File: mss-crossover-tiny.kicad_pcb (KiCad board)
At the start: 2 copper layers, 50.8 x 71.6 mm, 35 parts, among them J1 2x-screw, J2 RJ45, J3 2x-screw, J4 2x-screw, J5 ISP--5V, J6 TagConnect, J7 RJ45, SW1 Set, U1 L78M05CDT, U2 ACS724xLCTR-05AB, U3 ATtiny25-20SS, U4 AD8603, U5 LTV-355T

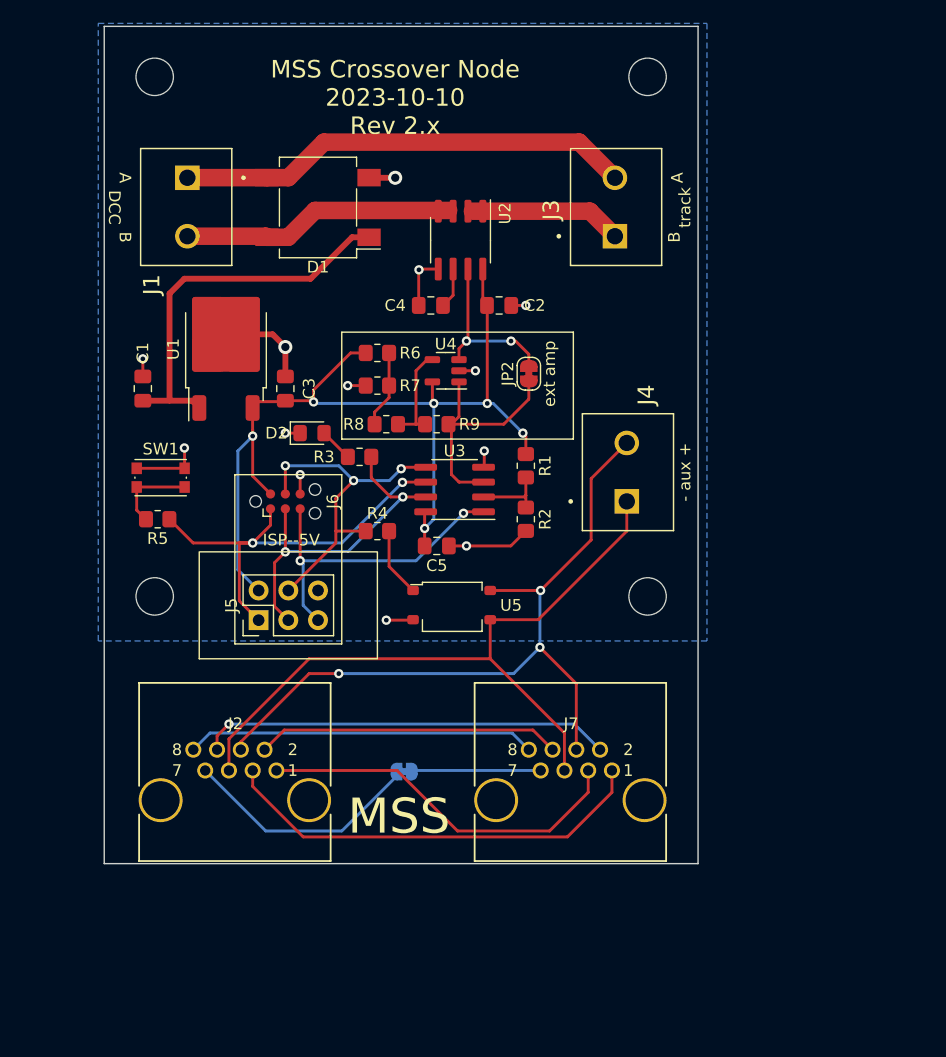
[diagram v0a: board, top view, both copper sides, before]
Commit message: Added test points to board.  In src, added code to control the opto-isolator as well as the LED.
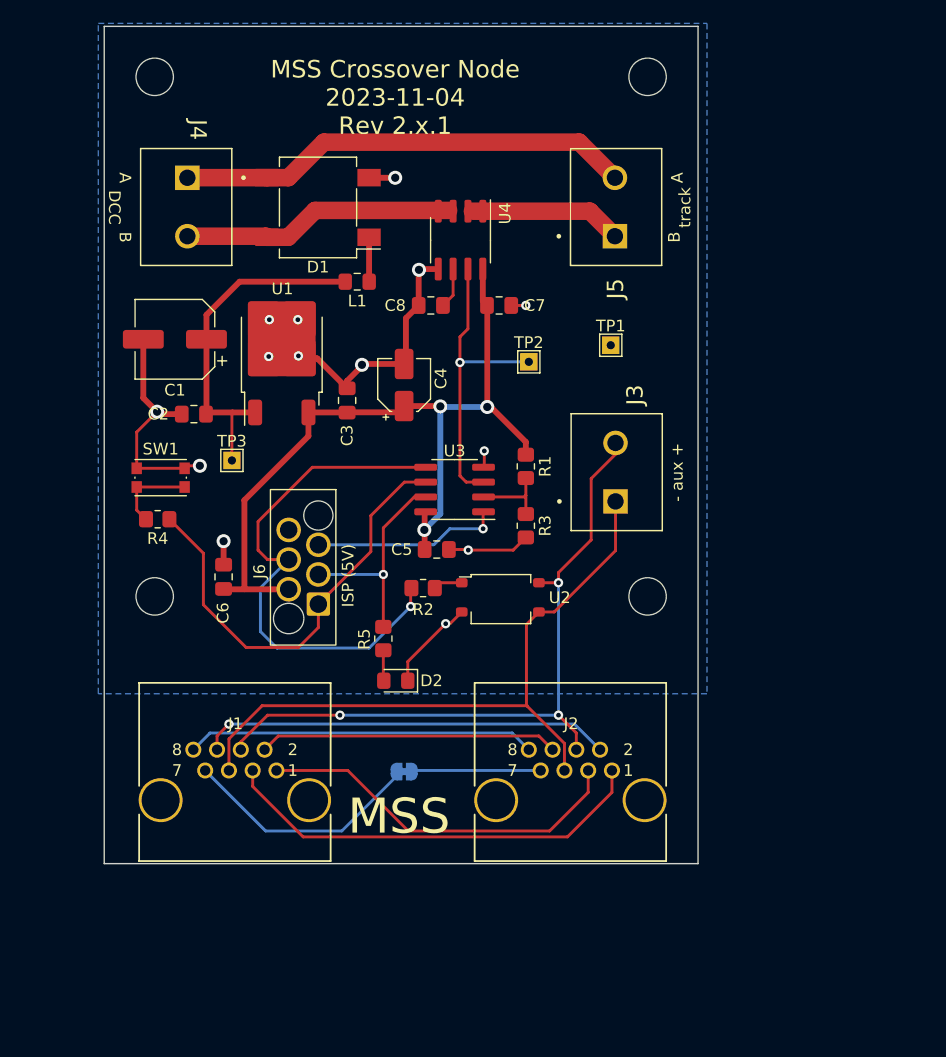
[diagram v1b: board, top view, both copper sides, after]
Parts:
- removed the J6 at (121.4, 96.3)
- removed JP2: ext amp, Jumper:SolderJumper-2_P1.3mm_Bridged_RoundedPad1.0x1.5mm
- removed R6, R7, R8, R9: 39k, Resistor_SMD:R_0805_2012Metric_Pad1.20x1.40mm_HandSolder
- removed the U4 at (135.1, 85.1)
- added C1: 47µF, Capacitor_SMD:CP_Elec_6.3x5.7, F.Cu at (112.0, 82.4)
- added C4: 10µF, Capacitor_SMD:CP_Elec_4x5.7, F.Cu at (131.6, 86.3)
- added C6: 100nF, Capacitor_SMD:C_0805_2012Metric_Pad1.18x1.45mm_HandSolder, F.Cu at (116.1, 102.7)
- added L1: L, Inductor_SMD:L_0805_2012Metric_Pad1.15x1.40mm_HandSolder, F.Cu at (127.6, 77.5)
- added TP1: TestPoint, TestPoint:TestPoint_THTPad_1.5x1.5mm_Drill0.7mm, F.Cu at (149.3, 82.9)
- added TP2: TestPoint, TestPoint:TestPoint_THTPad_1.5x1.5mm_Drill0.7mm, F.Cu at (142.2, 84.3)
- added TP3: TestPoint, TestPoint:TestPoint_THTPad_1.5x1.5mm_Drill0.7mm, F.Cu at (116.8, 92.8)
- C8: renamed from C4; value 1nF -> 3.3nF
- J6: renamed from J5; value ISP--5V -> ISP (5V); footprint myMods:PinHeader_2x03_P2.54mm_Vertical_Shrouded -> myMods:skedd-6-debugging
- R4: renamed from R5; value 2.2k -> 4.7k
- R5: renamed from R3; value 2.2k -> 4.7k
- moved D2 22.4 mm to (130.9, 111.6), turned to 180 degrees
- moved R5 15.7 mm to (129.8, 108.0), turned to -90 degrees
- moved R2 6.25 mm to (133.2, 103.7)
- moved C3 5.38 mm to (126.7, 87.6)
- moved J6 5.29 mm to (124.2, 105.1), turned to -90 degrees
- moved C2 4.88 mm to (113.6, 88.8), turned to 180 degrees
- moved U1 4.79 mm to (121.1, 83.6)
- moved U2 4.22 mm to (143.1, 103.2)
- moved J3 0.97 mm to (149.7, 96.3)
- moved R3 0.56 mm to (142.0, 98.3)
- moved C5 0.30 mm to (134.4, 100.4)
- moved R1 0.05 mm to (142.0, 93.3)
- renumbered C1 to C2, C2 to C7, J2 to J1, J7 to J2, J4 to J3, J1 to J4, J3 to J5, R4 to R2, R2 to R3, U5 to U2, U2 to U4
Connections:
- C2 pad 1: Net-(D1-+) -> Net-(U1-Input)
- U1 pad 1: Net-(D1-+) -> Net-(U1-Input)
- U3 pad 3: Net-(JP2-A) -> Net-(U3-XTAL2/PB4)
- U4 pad 7: Net-(JP2-B) -> Net-(U3-XTAL2/PB4)
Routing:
- net Net-(U1-Input): track 0.00 -> 29.9 mm
- net Net-(D1-+): track 33.3 -> 3.80 mm
- net Net-(U3-XTAL2/PB4): track 0.00 -> 26.1 mm, vias 0 -> 1
- net GND: track 40.2 -> 63.4 mm, vias 13 -> 14
- net Net-(JP2-A): track 20.2 -> 0.00 mm
- net /MOSI: track 29.7 -> 45.3 mm, vias 3 -> 1
- net Net-(JP2-B): track 14.9 -> 0.00 mm, vias 2 -> 0
- net +5V: track 82.4 -> 69.9 mm, vias 6 -> 3
- net /RST: track 27.6 -> 16.1 mm, vias 2 -> 1
- net /SCK: track 29.5 -> 18.7 mm, vias 2 -> 1
- net Net-(U4--): track 8.30 -> 0.00 mm
- net Net-(R6-Pad2): track 6.61 -> 0.00 mm
- net /Local A: track 64.6 -> 59.4 mm
- net Net-(R2-Pad1): track 5.93 -> 2.50 mm
- net /MSS GND: track 60.8 -> 57.7 mm
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
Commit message: Changed to be able to plug the crossover board into a cascade board.
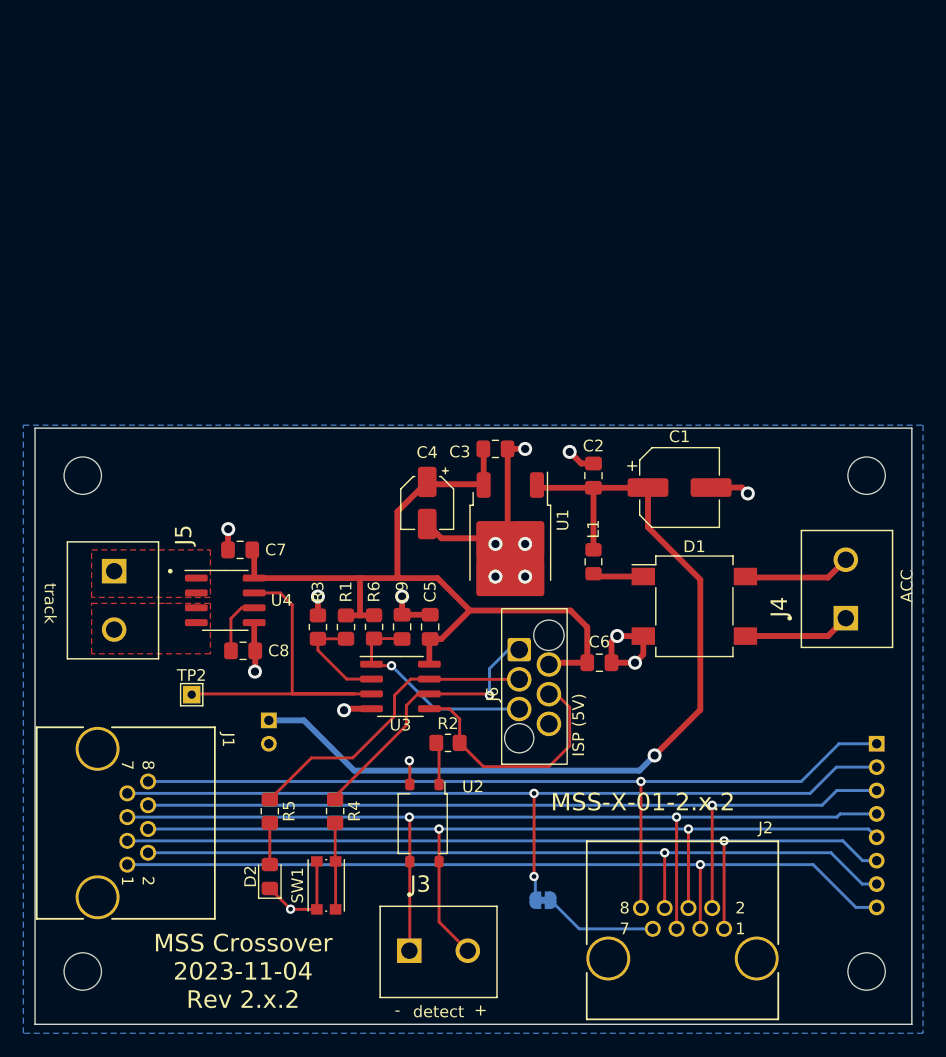
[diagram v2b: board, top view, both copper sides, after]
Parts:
- removed TP1, TP3: TestPoint, TestPoint:TestPoint_THTPad_1.5x1.5mm_Drill0.7mm
- added C9: 1uF, Capacitor_SMD:C_0805_2012Metric_Pad1.18x1.45mm_HandSolder, F.Cu at (131.4, 107.0)
- added J7: Conn_01x10_Pin, Connector_PinHeader_2.00mm:PinHeader_1x08_P2.00mm_Vertical, B.Cu at (172.0, 117.0)
- added J8: Conn_01x02_Pin, Connector_PinHeader_2.00mm:PinHeader_1x02_P2.00mm_Vertical, B.Cu at (120.0, 115.0)
- added R6: 10k, Resistor_SMD:R_0805_2012Metric_Pad1.20x1.40mm_HandSolder, F.Cu at (129.0, 107.0)
- moved J4 67.8 mm to (169.4, 106.3), turned to 90 degrees
- moved J5 51.5 mm to (106.8, 102.2), turned to -90 degrees
- moved D1 46.9 mm to (156.4, 105.2), turned to 0 degrees
- moved C1 45.0 mm to (155.1, 95.1), turned to 0 degrees
- moved J3 42.3 mm to (132.0, 134.7), turned to 0 degrees
- moved TP2 40.5 mm to (113.4, 112.8)
- moved REF** 38.9 mm to (171.1, 94.1)
- moved SW1 37.6 mm to (124.9, 129.1), turned to 90 degrees
- moved REF** 37.2 mm to (171.1, 136.5)
- moved U4 36.8 mm to (116.3, 104.7), turned to 0 degrees
- moved REF** 34.7 mm to (104.1, 94.1)
- moved C2 34.6 mm to (147.8, 94.1), turned to 90 degrees
- moved C8 33.6 mm to (117.8, 109.0), turned to 0 degrees
- moved C6 33.0 mm to (148.3, 110.1), turned to 180 degrees
- moved REF** 32.7 mm to (104.1, 136.5)
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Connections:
- net Net-(J5-Pin_1) renamed /t1
- net Net-(U1-Input) renamed +12V
- J5 pad 2: Net-(J4-Pin_1) -> /t2
- U4 pad 3: Net-(J4-Pin_2) -> /t2
- U4 pad 4: Net-(J4-Pin_2) -> /t2
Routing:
- net /7 A: track 20.8 -> 74.2 mm, vias 0 -> 2
- net +12V: track 29.9 -> 76.6 mm, vias 0 -> 1
- net /AD A: track 29.9 -> 74.5 mm, vias 0 -> 1
- net /Ain A: track 25.6 -> 68.2 mm, vias 0 -> 1
- net /AAin A: track 32.1 -> 71.1 mm, vias 0 -> 1
- net /Ain B: track 35.3 -> 71.6 mm
- net /AAin B: track 37.3 -> 72.3 mm, vias 0 -> 1
- net Net-(J4-Pin_1): track 39.1 -> 9.22 mm
- net /MSS GND: track 57.7 -> 85.2 mm, vias 0 -> 2
- net /MOSI: track 45.3 -> 21.5 mm, vias 1 -> 0
- net /Local A: track 59.4 -> 80.8 mm, vias 3 -> 2
- net /MISO: track 37.9 -> 23.6 mm, vias 0 -> 1
- net Net-(J4-Pin_2): track 23.3 -> 9.25 mm
- net /t1: track 13.1 -> 0.00 mm
- net /SCK: track 18.7 -> 26.7 mm, vias 1 -> 0
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- added copper zone on F.Cu, net /t1
- added copper zone on F.Cu, net /t2
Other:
- board size 50.8 x 71.6 mm -> 75 x 51 mm
- board text added: "MSS Crossover ${ISSUE_DATE} Rev ${REVISION}"
- board text added: "MSS-X-01-${REVISION}"
- board text removed: "MSS"
- board text removed: "MSS Crossover Node ${ISSUE_DATE} Rev ${REVISION}"

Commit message: Little updates.  Moved power from 12V to ACC back to 12V.
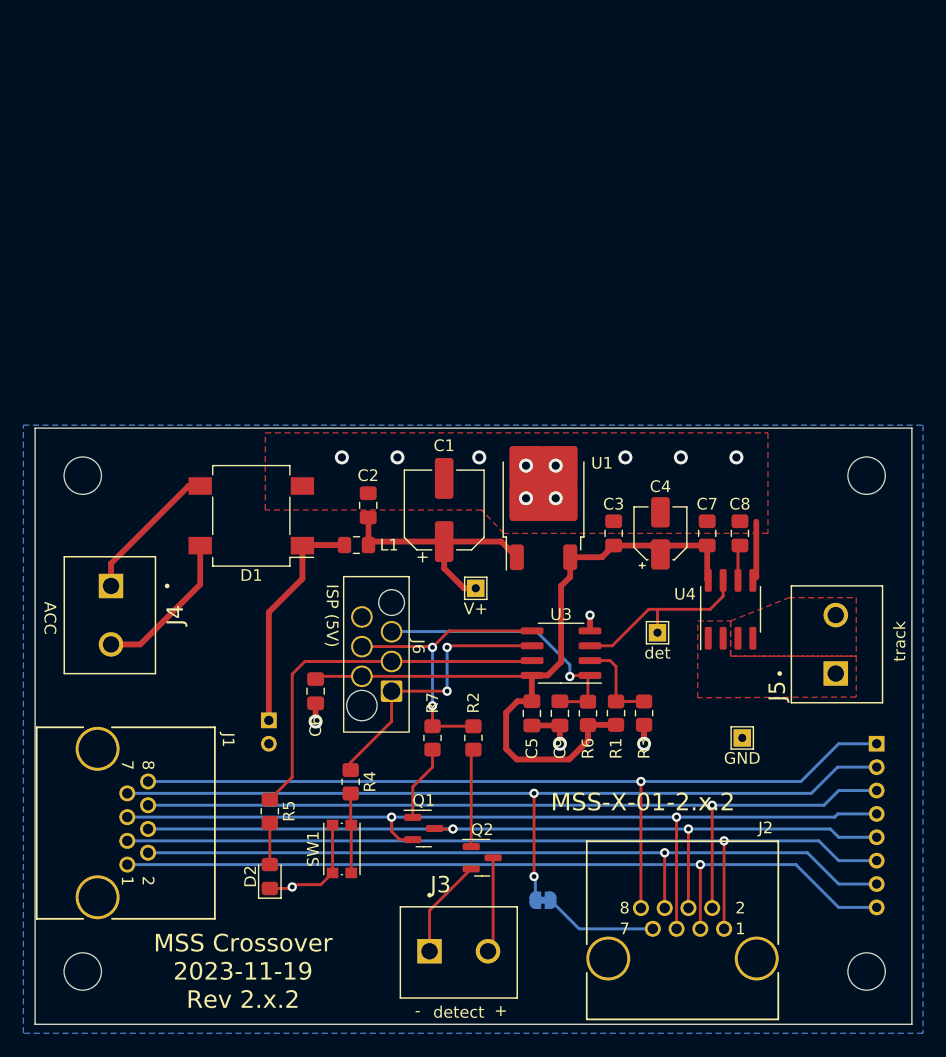
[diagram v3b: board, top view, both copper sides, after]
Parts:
- removed U2: LTV-355T, myMods:LTV-355T
- added Q1: 2N3904, Package_TO_SOT_SMD:SOT-23, F.Cu at (133.2, 124.2)
- added Q2: 2N3904, Package_TO_SOT_SMD:SOT-23, F.Cu at (138.2, 126.8)
- added R7: 2.2k, Resistor_SMD:R_0805_2012Metric_Pad1.20x1.40mm_HandSolder, F.Cu at (134.0, 116.5)
- added TP1: GND, TestPoint:TestPoint_THTPad_1.5x1.5mm_Drill0.7mm, F.Cu at (160.5, 116.5)
- added TP3: V+, TestPoint:TestPoint_THTPad_1.5x1.5mm_Drill0.7mm, F.Cu at (137.7, 103.7)
- R2: value 1k -> 2.2k
- TP2: value TestPoint -> det
- moved J4 62.9 mm to (106.5, 103.5), turned to -90 degrees
- moved J5 62.4 mm to (168.5, 111.0), turned to 90 degrees
- moved C8 43.7 mm to (160.3, 99.0), turned to 90 degrees
- moved U4 43.2 mm to (159.5, 105.5), turned to 90 degrees
- moved TP2 40.2 mm to (153.2, 107.5)
- moved C7 40.0 mm to (157.5, 99.0), turned to -90 degrees
- moved D1 38.7 mm to (118.5, 97.5), turned to 180 degrees
- moved R3 28.9 mm to (152.1, 114.4), turned to -90 degrees
- moved C6 24.4 mm to (124.0, 112.5), turned to 90 degrees
- moved R1 24.2 mm to (149.7, 114.4), turned to 90 degrees
- moved L1 20.3 mm to (127.5, 100.0), turned to 0 degrees
- moved C1 20.2 mm to (135.0, 97.0), turned to 90 degrees
- moved C4 20.1 mm to (153.5, 99.0), turned to 90 degrees
- moved R6 19.7 mm to (147.3, 114.4), turned to 90 degrees
- moved C2 19.4 mm to (128.5, 96.6)
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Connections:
- C1 pad 1: +12V -> Net-(U1-Input)
- C2 pad 1: +12V -> Net-(U1-Input)
- J1 pad 5: /MSS GND -> GND
- J2 pad 5: /MSS GND -> GND
- J3 pad 1: /MSS GND -> GND
- J3 pad 2: /Local A -> Net-(J3-Pin_2)
- J7 pad 4: /MSS GND -> GND
- J8 pad 1: +12V -> Net-(D1-+)
- L1 pad 2: +12V -> Net-(U1-Input)
- R2 pad 1: Net-(R2-Pad1) -> /MOSI
- R2 pad 2: /MOSI -> Net-(Q2-B)
- U1 pad 1: +12V -> Net-(U1-Input)
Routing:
- net /MSS GND: track 85.2 -> 0.00 mm, vias 2 -> 0
- net +12V: track 76.6 -> 0.00 mm, vias 1 -> 0
- net GND: track 56.9 -> 109.3 mm, vias 16 -> 17
- net Net-(U1-Input): track 0.00 -> 21.5 mm
- net Net-(U3-XTAL2/PB4): track 32.0 -> 16.5 mm
- net Net-(D1-+): track 4.36 -> 19.8 mm
- net /Local A: track 80.8 -> 71.0 mm
- net Net-(Q2-B): track 0.00 -> 8.38 mm
- net Net-(J3-Pin_2): track 0.00 -> 8.18 mm
- net Net-(Q1-B): track 0.00 -> 6.50 mm
- net /SCK: track 26.7 -> 32.5 mm
- net /RST: track 18.9 -> 23.5 mm
- net /MOSI: track 21.5 -> 25.4 mm, vias 0 -> 2
- net Net-(J4-Pin_2): track 9.25 -> 13.1 mm
- net Net-(R2-Pad1): track 3.66 -> 0.00 mm
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- added copper zone on F.Cu, net GND

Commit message: Reworked design to use a current shunt instead.
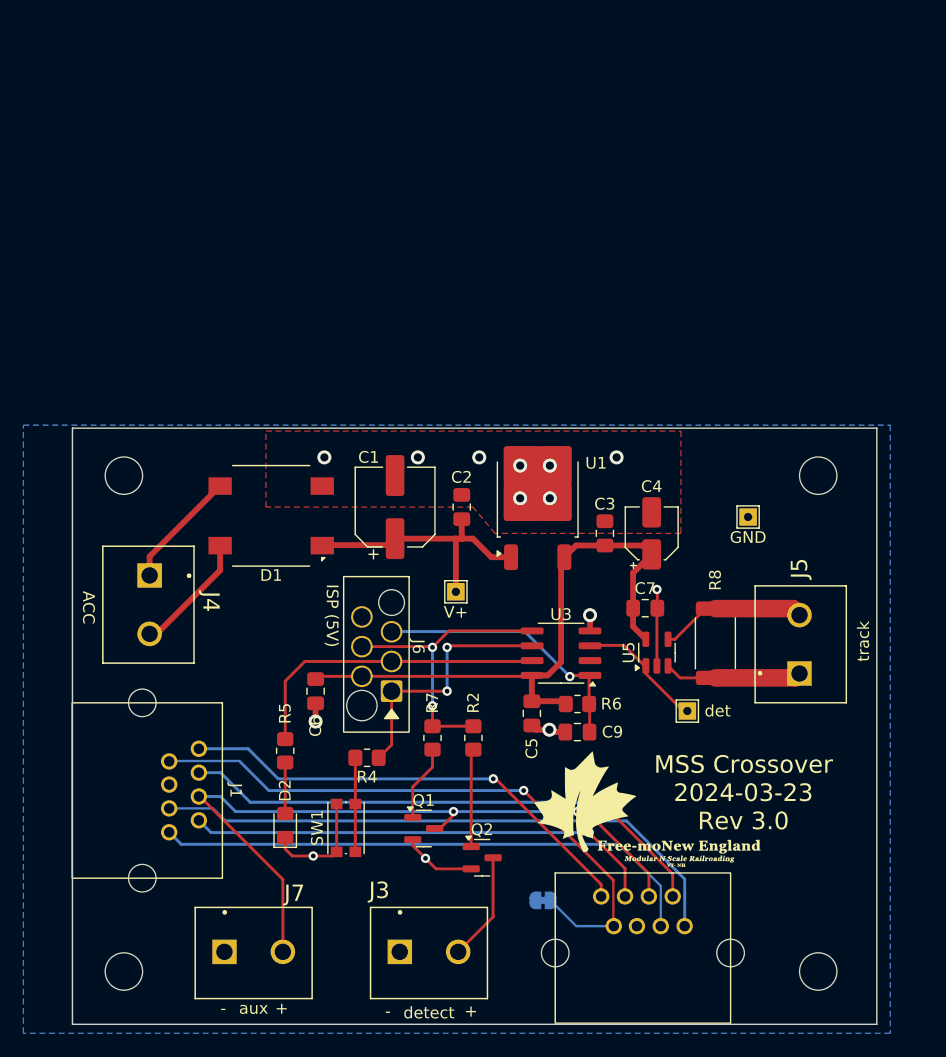
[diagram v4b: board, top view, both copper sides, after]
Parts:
- removed C8: 3.3nF, Capacitor_SMD:C_0805_2012Metric_Pad1.18x1.45mm_HandSolder
- removed J8: Conn_01x02_Pin, Connector_PinHeader_2.00mm:PinHeader_1x02_P2.00mm_Vertical
- removed L1: L, Inductor_SMD:L_0805_2012Metric_Pad1.15x1.40mm_HandSolder
- removed R1, R3: 39k, Resistor_SMD:R_0805_2012Metric_Pad1.20x1.40mm_HandSolder
- removed U4: ACS724xLCTR-05AB, Package_SO:SOIC-8_3.9x4.9mm_P1.27mm
- added G***: LOGO, myMods:Free-moNH-20, F.Cu at (152.3, 122.9)
- added R8: 0.1 3W, Resistor_SMD:R_2512_6332Metric, F.Cu at (158.2, 108.4)
- added U5: INA180A3, Package_TO_SOT_SMD:SOT-23-5, F.Cu at (153.2, 109.2)
- C1: value 47µF -> 100µF; footprint Capacitor_SMD:CP_Elec_6.3x5.7 -> Capacitor_SMD:CP_Elec_6.3x7.7
- C2: value .33uF -> .33µF
- J1, J2: footprint Imports:CONN_RJSBE5080_16P13X12P57_AMP -> myMods:MJ3221-88
- J7: value Conn_01x10_Pin -> 2x-screw; footprint Connector_PinHeader_2.00mm:PinHeader_1x08_P2.00mm_Vertical -> Imports:CUI_TB003-500-P02BE; moved to F.Cu
- moved J7 58.6 mm to (116.2, 134.8), turned to 0 degrees
- moved TP1 18.9 mm to (161.0, 97.6)
- moved C7 8.31 mm to (152.2, 105.4), turned to 0 degrees
- moved C2 8.00 mm to (136.5, 96.8)
- moved J1 7.28 mm to (111.5, 121.0)
- moved TP2 7.17 mm to (155.8, 114.2)
- moved J2 6.95 mm to (152.0, 132.6)
- moved R5 5.33 mm to (121.4, 117.6)
- moved D2 4.55 mm to (121.4, 124.0)
- moved C1 4.21 mm to (130.8, 96.8)
- moved REF** 4.14 mm to (167.0, 94.1)
- moved REF** 4.14 mm to (167.0, 136.5)
- moved REF** 3.52 mm to (107.6, 136.5)
- moved REF** 3.52 mm to (107.6, 94.1)
- moved J4 3.42 mm to (109.8, 102.6)
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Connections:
- C1 pad 1: Net-(U1-Input) -> Net-(D1-+)
- C2 pad 1: Net-(U1-Input) -> Net-(D1-+)
- C7 pad 1: GND -> +5V
- C7 pad 2: +5V -> GND
- J2 pad 7: /7 B -> /7 A
- J5 pad 1: /t1 -> Net-(J5-Pin_1)
- J5 pad 2: /t2 -> Net-(J5-Pin_2)
- J7 pad 1: /AD A -> GND
- J7 pad 2: /7 A -> /Local A
- JP1 pad 1: /7 B -> GND
- TP3 pad 1: Net-(U1-Input) -> Net-(D1-+)
- U1 pad 1: Net-(U1-Input) -> Net-(D1-+)
- U3 pad 2: Net-(U3-XTAL1/PB3) -> unconnected-(U3-XTAL1/PB3-Pad2)
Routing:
- net GND: track 109.3 -> 28.8 mm, vias 17 -> 14
- net /AD A: track 74.5 -> 40.2 mm
- net /Ain A: track 68.2 -> 40.6 mm
- net /Ain B: track 71.6 -> 46.0 mm
- net /AAin A: track 71.1 -> 47.4 mm, vias 1 -> 0
- net /7 A: track 74.2 -> 52.5 mm, vias 2 -> 1
- net /AAin B: track 72.3 -> 50.6 mm, vias 1 -> 0
- net Net-(U1-Input): track 21.5 -> 0.00 mm
- net +5V: track 65.9 -> 52.0 mm
- net Net-(J5-Pin_2): track 0.00 -> 12.6 mm
- net Net-(J5-Pin_1): track 0.00 -> 11.8 mm
- net /7 B: track 9.76 -> 0.00 mm
- net /Local A: track 71.0 -> 62.0 mm
- net Net-(U3-XTAL1/PB3): track 7.39 -> 0.00 mm
- net /SCK: track 32.5 -> 26.8 mm
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- removed copper zone on F.Cu, net /t1
- removed copper zone on F.Cu, net /t2
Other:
- board size 75 x 51 mm -> 68.8 x 51 mm
- board text removed: "MSS-X-01-${REVISION}"
